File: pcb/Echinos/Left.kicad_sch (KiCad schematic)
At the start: 38 parts, among them J1 USB_C_Receptacle_USB2.0, J2 TagConnect_6pins, J3 Pogo, J4 Conn_01x12_Socket, SW1 SW_Push, SW2 SW_Push, U2 W25Q128JVS, U4 USBLC6-2P6, U5 XC6210B332MR-G

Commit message: ✨ ♻️ 🚧 [PCB] - Continue draft schematic by adding LCSC parts / footprint assignation. Integration of trackball schematic.
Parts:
- added D2: TPD1E10B06-Q1, Diode_SMD:D_SOD-523, symbol Diode:BZT52Bxx
- added U4: ESD7L5.0DT5G-N, Echinos:D_TVS_SOT-723, symbol Power_Protection:TPD2EUSB30
- R1, R10, R11, R13: footprint Resistor_SMD:R_0402_1005Metric_Pad0.72x0.64mm_HandSolder -> Resistor_SMD:R_0805_2012Metric_Pad1.20x1.40mm_HandSolder; LCSC C269746 -> C413739
- SW1: value SW_Push -> Reset
- SW2: value SW_Push -> Bootloader
- renumbered H9 to H6, H6 to H7, H7 to H8, H8 to H9
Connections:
- net Earth is gone; now on an unnamed net: J1.S1 (SHIELD)
- net GND: now also FB1.2, D2.2 (A), U4.3 (GND)
- net USB_D+: now also U4.1 (D+)
- net USB_D-: now also U4.2 (D-)
- net VBUS: now also D2.1 (K)
- net ~{USB_BOOT}: no longer names the net of R5.1, SW2.2
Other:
- added sheet Trackball_Left (Trackball.kicad_sch)
- note added: "1) EMI shield 2) Use a ferrite bead to protect against high frequency 3) Floating to avoid canceling host shield protection Always force a unique path to ground if connected to ground"
- note added: "Bootloader / Reset buttons"
- note added: "ESD protection - VBUS + IO --> ElecSuper USBLC6-2P6-ES (5V, 3 lines, SOT-563) - VBUS --> Texas Instruments TVS0500DRVR (0.39) --> Texas Instruments TPD1E10B06QDPYRQ1 (1.11) - IO --> Born ESD7L5.0DT5G-N (5V, 2 lines, SOT 723) (0.13) --> Texas Instruments TPD2E2U06 (TODO)"
- note added: "Halves communication"
- note added: "I2C Pullers (Optional)"
- note added: "Information"
- note added: "Keyboard matrix"
- note added: "Packaging (metric | imperial) - Resistors - RP2040 --> 1005 | 402 - I2C puller --> 2012 | 805 - Capacitors - RP2040 --> 0402 | 1005 - Diodes - Switches --> SOD-123 - TVS --> SOD-523 - Transistors - ESD --> SOT-723"
- note added: "Trackball (SPI 1)"
- note added: "Trackpad / Trackball (SPI / I2C 0)"
- note removed: "1) Create an all-round contact point between the PCB and the metal housing --> EMI shield 2) Use a ferrite bead to protect against high frequency and force a unique path to ground 3) Avoid any connection (floating) to avoid canceling host shield protection"
- note removed: "??? I2C ???"
- note removed: "Boot / Reset buttons"
- note removed: "Connection between halves"
- note removed: "Matrix"
- note removed: "Trackball / Trackpad (SPI)"
- title: Left Side -> Echinos - Left Side
- moved on the sheet: C14, C18, C19, D1, D2, F1, FB1, H1, H2, H3, H4, H5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

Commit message: ✨ [PCB] - Continue draft schematic by adding per key RGB LED.
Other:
- sheet Matrix_Left ports: added rgb_keys; removed none
- note added: "Keyboard matrix (Keys / LEDs)"
- note added: "Packaging (metric | imperial) - Resistors - RP2040 --> 1005 | 0402 - I2C puller --> 2012 | 0805 - Others --> 1608 | 0603 - Capacitors - RP2040 --> 1005 | 0402 - Others --> 1608 | 0603 - Diodes - Switches --> SOD-123 - TVS --> SOD-523 - Transistors - ESD --> SOT-723"
- note added: "Trackball (SPI 0) --- SPI - motion = Active low interupt line"
- note added: "Trackball sensor directly on the PCB - Minimize the keyboard total height - Enough place for a 34mm ball - Use SPI 1 leaving SPI 0 exposed with the FPC connector"
- note added: "Trackpad (SPI 0 / I2C 0)"
- note added: "Trackpad (SPI 0 / I2C 0) --- SPI - motion = Data Ready (DR) line I2C - Remove R1 on the trackpad PCB"
- note removed: "Keyboard matrix"
- note removed: "Packaging (metric | imperial) - Resistors - RP2040 --> 1005 | 402 - I2C puller --> 2012 | 805 - Capacitors - RP2040 --> 0402 | 1005 - Diodes - Switches --> SOD-123 - TVS --> SOD-523 - Transistors - ESD --> SOT-723"
- note removed: "Trackpad / Trackball (SPI / I2C 0)"
- note removed: "VCC options - 3V and remove R1 to Trackpad PCB - 5V and remove R1/R7/R8 to Trackpad PCB R1 removed --> I2C connection R7/R8 removed --> Support for 5V power"
- note removed: "motion line: - Trackball --> Active low interupt line (motion pin) - Trackpad --> SPI Data ready pin (DR pin)"
- moved on the sheet: D2, H1, H2, H3, H4, H5, H6, H7, H8, H9, J2, J4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

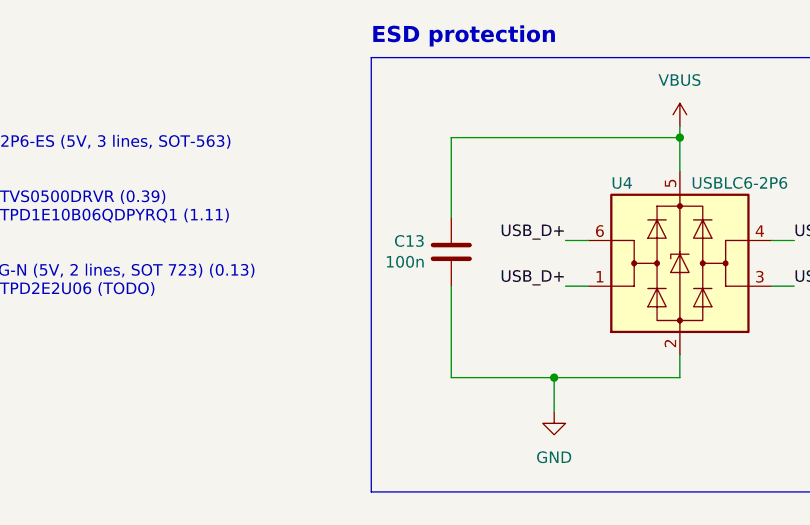
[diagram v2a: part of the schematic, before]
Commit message: ♻️ [PCB] - Remove symbol instances linking to other projets due to copy and paste of component symbol.
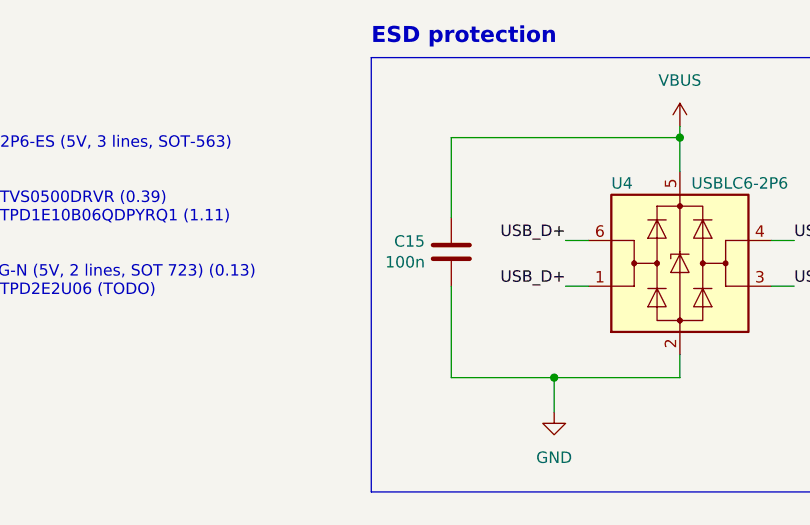
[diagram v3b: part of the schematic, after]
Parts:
- renumbered C13 to C15
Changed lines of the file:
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@@
-        )
-      )
-      (project "ptechinos"
-        (path "/e63e39d7-6ac0-4ffd-8aa3-1841a4541b55"
-          (reference "H1") (unit 1)
         )
       )
@@
   (symbol (lib_id "Device:C") (at -52.07 -48.26 0) (mirror y) (unit 1)
     (in_bom yes) (on_board yes) (dnp no)
-    (property "Reference" "C13" (at -54.991 -49.4284 0)
+    (property "Reference" "C15" (at -54.991 -49.4284 0)
       (effects (font (size 1.27 1.27)) (justify left))
     )
@@
     (pin "2")
     (instances
-      (project "RP2040_minimal"
-        (path "/4f77defa-fbfc-4ef8-94fc-c086dd0772f3"
-          (reference "C13") (unit 1)
-        )
-      )
       (project "Echinos"
         (path "/5bd3006d-ec09-4ffb-bec3-03fa5613b46a"
@@
         )
       )
-      (project "ptechinos"
-        (path "/e63e39d7-6ac0-4ffd-8aa3-1841a4541b55"
-          (reference "H9") (unit 1)
-        )
-      )
     )
   )
@@
         )
       )
-      (project "ptechinos"
-        (path "/e63e39d7-6ac0-4ffd-8aa3-1841a4541b55"
-          (reference "H5") (unit 1)
-        )
-      )
     )
   )
@@
         )
       )
-      (project "ptechinos"
-        (path "/e63e39d7-6ac0-4ffd-8aa3-1841a4541b55"
-          (reference "H2") (unit 1)
-        )
-      )
     )
   )
@@
       (project "Echinos"
         (path "/5bd3006d-ec09-4ffb-bec3-03fa5613b46a/82089e05-aeac-4bc0-b466-29ce28ef1ab1"
-          (reference "H4") (unit 1)
-        )
-      )
-      (project "ptechinos"
-        (path "/e63e39d7-6ac0-4ffd-8aa3-1841a4541b55"
           (reference "H4") (unit 1)
         )
@@
         )
       )
-      (project "ptechinos"
-        (path "/e63e39d7-6ac0-4ffd-8aa3-1841a4541b55"
-          (reference "J7") (unit 1)
-        )
-      )
     )
   )
@@
         )
       )
-      (project "ptechinos"
-        (path "/e63e39d7-6ac0-4ffd-8aa3-1841a4541b55"
-          (reference "H3") (unit 1)
-        )
-      )
     )
   )
@@
         )
       )
-      (project "ptechinos"
-        (path "/e63e39d7-6ac0-4ffd-8aa3-1841a4541b55"
-          (reference "H7") (unit 1)
-        )
-      )
     )
   )
@@
       (project "Echinos"
         (path "/5bd3006d-ec09-4ffb-bec3-03fa5613b46a/82089e05-aeac-4bc0-b466-29ce28ef1ab1"
-          (reference "H8") (unit 1)
-        )
-      )
-      (project "ptechinos"
-        (path "/e63e39d7-6ac0-4ffd-8aa3-1841a4541b55"
           (reference "H8") (unit 1)
         )
@@
           (reference "H6") (unit 1)
         )
-      )
-      (project "ptechinos"
-        (path "/e63e39d7-6ac0-4ffd-8aa3-1841a4541b55"
-          (reference "H6") (unit 1)
-        )

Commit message: ♻️ [PCB] - Add ferrite bead between shield and ground. Assign hand solder footprints whenever possible. Complete footprint assignation.
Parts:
- C14, C18, C19: footprint Capacitor_SMD:C_0603_1608Metric -> Capacitor_SMD:C_0603_1608Metric_Pad1.08x0.95mm_HandSolder
- C15: footprint Capacitor_SMD:C_0402_1005Metric -> Capacitor_SMD:C_0402_1005Metric_Pad0.74x0.62mm_HandSolder
- D1: footprint (none) -> Diode_SMD:D_SOD-323_HandSoldering
- D2: footprint Diode_SMD:D_SOD-323 -> Diode_SMD:D_SOD-323_HandSoldering
- F1: footprint Fuse:Fuse_0603_1608Metric -> Fuse:Fuse_0603_1608Metric_Pad1.05x0.95mm_HandSolder
- FB1: value FerriteBead_Small -> 80@100Mhz; footprint (none) -> Inductor_SMD:L_0805_2012Metric_Pad1.15x1.40mm_HandSolder; LCSC C98288 -> C12389
- J1: footprint (none) -> Connector_USB:USB_C_Receptacle_HRO_TYPE-C-31-M-12; LCSC (none) -> C165948
- JP1, JP2: footprint (none) -> Echinos:SolderJumper_Open_0.8x1.2mm
- R2, R3, R4, R5, R9: footprint Resistor_SMD:R_0402_1005Metric -> Resistor_SMD:R_0402_1005Metric_Pad0.72x0.64mm_HandSolder
- U5: footprint Package_TO_SOT_SMD:SOT-23-5 -> Package_TO_SOT_SMD:SOT-23-5_HandSoldering
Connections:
- net +5V: now also D2.1 (K)
- net GND: now also FB1.1; no longer FB1.2
- net VBUS: no longer D2.1 (K), F1.1, J1.A4 (VBUS), J1.A9 (VBUS), J1.B4 (VBUS), J1.B9 (VBUS)
- net Earth: now reaches J1.S1 (SHIELD)
- net Earth: now also FB1.2; no longer FB1.1
- new net: F1.1, J1.A4 (VBUS), J1.A9 (VBUS), J1.B4 (VBUS), J1.B9 (VBUS)
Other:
- note added: "Design rules ---------"
- note added: "Filter ESD (100-500Mhz) Filter high frequency noise Impedance should be in 50-100Ω range at 100Mhz Impedance drop quickly when moving toward ferrite current rating --> I_Circuit ~= 0.2 x I_CR Continue USB Shield using metalic case / plate to create a 360° protection Connect Shield and Ground in only one location (keep out one under USB)"
- note added: "Packaging (metric | imperial) - Resistors - RP2040 --> 1005 | 0402 - USB data --> 1005 | 0402 - I2C puller --> 2012 | 0805 - Others --> 1608 | 0603 - Capacitors - RP2040 --> 1005 | 0402 - Others --> 1608 | 0603 - Diodes - Switches --> SOD-123 - TVS --> SOD-523 - Transistors - ESD --> SOT-723"
- note added: "Tells host that we need 500mA"
- note removed: "1) EMI shield 2) Use a ferrite bead to protect against high frequency 3) Floating to avoid canceling host shield protection Always force a unique path to ground if connected to ground"
- note removed: "Packaging (metric | imperial) - Resistors - RP2040 --> 1005 | 0402 - I2C puller --> 2012 | 0805 - Others --> 1608 | 0603 - Capacitors - RP2040 --> 1005 | 0402 - Others --> 1608 | 0603 - Diodes - Switches --> SOD-123 - TVS --> SOD-523 - Transistors - ESD --> SOT-723"
- moved on the sheet: D2, F1, J1, R2, R3

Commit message: ✨ 🐛 ✅ [PCB] - Pass ERC test (exception to unconnected GPIO pins). Fix power symbol assignation to please Kicad. Fix duplicated line name (encoder / joystick) to please Kicad. Add trackball sensor connection documentation. Assign newly created footprints (encoder, joystick, switch).
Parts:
- removed C15: 100n, Capacitor_SMD:C_0402_1005Metric_Pad0.74x0.62mm_HandSolder, symbol Device:C
- removed U4: USBLC6-2P6, Package_TO_SOT_SMD:SOT-666, symbol Power_Protection:USBLC6-2P6
- H6: symbol ptechinos:Mount_Tenting -> Echinos:Mount_Tenting; now in the parts list
- J3: footprint Echinos:Pogo_1x04_P2.5mm -> Echinos:Pogo_RightAngle_1x04_P2.5mm
- SW1: value Reset -> SW_Push
- SW2: value Bootloader -> SW_Push
- renumbered U4 to U3
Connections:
- net +3V3 is gone; now on net +3.3V: C19.1, J3.1 (Pin_1), J4.12 (Pin_12), JP1.1 (A), JP2.1 (A), R12.2, R9.1, U5.5 (VOUT)

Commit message: ✨ [PCB] - Complete schema and PCB for left halve. All connections are made. Optional encoder on the top outer key Optional joystick on either outer thumb or above middle thumb. Optional power LED (jumpers) SATA to connect both sides VIK compatible (except for 5.0V track) with enough space on the inner side to clip a VIK module Remaining MCU pins exposed with a 2.54mm spaced header All VIK modules are not yet placed / routed.
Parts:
- removed H6: Mount_Tenting, Echinos:Tenting_Puck, symbol Echinos:Mount_Tenting
- removed J3: Pogo, Echinos:Pogo_RightAngle_1x04_P2.5mm, symbol Connector_Generic:Conn_01x04
- added FB1: 80@100Mhz, Inductor_SMD:L_0805_2012Metric_Pad1.15x1.40mm_HandSolder, symbol Device:FerriteBead_Small
- added J205: ~, symbol Vik:vik-module-connector
- added J206: Conn_01x06_Pin, Connector_PinHeader_2.54mm:PinHeader_1x06_P2.54mm_Vertical, symbol Connector:Conn_01x06_Pin
- added J301: SATA-7p, Echinos:SATA_1x07_P1.27mm_SMD, symbol Echinos:SATA-7p
- added JP2: 3x3_LED_jumper, Echinos:SolderJumper_Open_0.8x1.2mm, symbol Jumper:SolderJumper_2_Open
- added U7: D3V3F4U6S-7, Echinos:D_TVS_SOT-363, symbol Echinos:D3V3F4U6S-7
- H1, H2, H3, H4, H5: footprint MountingHole:MountingHole_3.2mm_M3_Pad_Via -> Echinos:MountingHole_3mm_Pad_Via; symbol Mechanical:MountingHole -> Mechanical:MountingHole_Pad
- J4: value Conn_01x12_Socket -> FPC_VIK
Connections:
- net +3.3V: now also J4.1 (Pin_1), J205.12 (3V3), J206.2 (Pin_2), J301.2 (S2), J301.3 (S3), JP2.1 (A), U7.2 (VN); no longer J4.12 (Pin_12), R12.2
- net GND: now also H1.1, H2.1, H3.1, H4.1, H5.1, J4.2 (Pin_2), SW1.2, FB1.2, J205.11 (GND), J206.1 (Pin_1), J301.1 (S1), J301.4 (S4), J301.7 (S7), U7.5 (VP); no longer J4.11 (Pin_11), SW1.1
- net USB_D+: now also U3.2 (D+); no longer U3.1 (D+)
- net USB_D-: now also U3.1 (D-); no longer U3.2 (D-)
- net adc_2: now also J4.9 (Pin_9), J205.4 (GPIO_AD2)
- net adc_3: now also J4.7 (Pin_7), J205.6 (GPIO_AD1)
- net csn0: now also J206.6 (Pin_6); no longer J4.3 (Pin_3)
- net csn1: now also J4.10 (Pin_10), J205.3 (SPI_CS)
- net miso0: now also J206.5 (Pin_5); no longer J4.2 (Pin_2)
- net miso1: now also J4.11 (Pin_11), J205.2 (MISO)
- net mosi0: now also J206.4 (Pin_4); no longer J4.5 (Pin_5)
- net mosi1: now also J4.8 (Pin_8), J205.5 (MOSI)
- net motion: no longer J4.4 (Pin_4)
- net sck0: now also J206.3 (Pin_3); no longer J4.1 (Pin_1)
- net sck1: now also J4.12 (Pin_12), J205.1 (SCLK)
- net scl0: no longer J4.9 (Pin_9)
- net scl1: now also J4.4 (Pin_4), J205.9 (SCL)
- net sda0: no longer J4.10 (Pin_10)
- net sda1: now also J4.3 (Pin_3), J205.10 (SDA)
- net ~{RST}: now also SW1.1; no longer SW1.2
- net VBUS: now reaches F1.1, J1.A4 (VBUS), J1.A9 (VBUS), J1.B4 (VBUS), J1.B9 (VBUS)
- new net: JP2.2 (B), R12.2
- new net: FB1.1, J301.SH1 (SHIELD), J301.SH2 (SHIELD)
- new net RX: J301.5 (S5), U7.1 (CH1), U7.3 (CH2)
- new net TX: J301.6 (S6), U7.4 (CH3), U7.6 (CH4)
- new net rgb: J205.8 (RGB_LED_IN), J4.5 (Pin_5)
- no-connect marks 7 -> 5
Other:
- sheet Matrix_Left ports: added backlights; removed rgb_keys
- sheet RP2040_Left ports: added GPIO4, VBUS_DET; removed GPI04, GPIO7
- note added: "EMI Shield / Case mounting holes"
- note added: "ESD protection (USB + SATA)"
- note added: "I2C --> Remove R1 on the trackpad PCB"
- note added: "Resistor must be close to the flash chip Switch pushed (low) --> Bootloader Switch released (pulled high) --> Firmware"
- note added: "SATA (3.3V, USART)"
- note added: "Trackpad (SPI 1 or I2C 1)"
- note added: "USART full duplex RX_left <-- TX_right TX_left --> RX_right"
- note added: "USB (5.5V, Data)"
- note added: "Unused MCU pins"
- note added: "VIK compatible - Cirque compatible with FPC Type A cable (reverse pins) ?? 5V is a waste pin that could be used to expose another IO ?? ?? - Could be useful with a joystick ??"
- note added: "VIK connector (SPI 1 / I2C 1)"
- note added: "VIK modules"
- note removed: "??? EMI Shield / Case mounting holes ???"
- note removed: "??? OLED / LCD ???"
- note removed: "??? TRRS ???"
- note removed: "ESD protection"
- note removed: "Resistor must be close to the flash chip Switch pushed (low) --> USB Bootloader Switch released (pulled high) --> Firmware"
- note removed: "Trackball sensor directly on the PCB - Minimize the keyboard total height - Enough place for a 34mm ball - Use SPI 1 leaving SPI 0 exposed with the FPC connector"
- note removed: "Trackpad (SPI 0 / I2C 0)"
- moved on the sheet: D1, D2, H7, H8, H9, J4, JP1, JP2, R1, R10, R11, R12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

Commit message: 🚧 [PCB] - Backup of a specific layout around MCU. Modules moved to a specific schematic page.
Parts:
- removed H7, H8, H9: GuardHole, MountingHole:MountingHole_2.2mm_M2_Pad_Via, symbol Mechanical:MountingHole
- removed J205: ~, symbol Vik:vik-module-connector
- added J208: FPC (PCB), Connector_FFC-FPC:Hirose_FH12-12S-0.5SH_1x12-1MP_P0.50mm_Horizontal, symbol Connector:Conn_01x12_Socket
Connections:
- net +3.3V: now also J208.11 (Pin_11)
- net GND: now also J208.12 (Pin_12)
- net adc_0: now also J208.9 (Pin_9)
- net adc_1: now also J208.7 (Pin_7)
- net col1: now also J208.1 (Pin_1)
- net col2: now also J208.2 (Pin_2)
- net col3: now also J208.3 (Pin_3)
- net col4: now also J208.4 (Pin_4)
- net col5: now also J208.6 (Pin_6)
- net rgb: now also J208.8 (Pin_8)
- new net row5: J208.5 (Pin_5)
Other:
- removed sheet Trackball_Left
- note added: "EMI Shield Case mounting holes"
- note added: "Expansion connector (Matrix / ADC)"
- note added: "Matrix diodes must be added on the module side."
- note added: "Matrix expansion - Add 5 way joystick - Add mouse buttons - ..."
- note added: "Unused MCU pins (Optional)"
- note removed: "??? Design / Artist ???"
- note removed: "EMI Shield / Case mounting holes"
- note removed: "I2C --> Remove R1 on the trackpad PCB"
- note removed: "Trackball (SPI 0) --- SPI - motion = Active low interupt line"
- note removed: "Trackball (SPI 1)"
- note removed: "Trackpad (SPI 0 / I2C 0) --- SPI - motion = Data Ready (DR) line I2C - Remove R1 on the trackpad PCB"
- note removed: "Trackpad (SPI 1 or I2C 1)"
- note removed: "Unused MCU pins"
- note removed: "VIK modules"
- moved on the sheet: H1, H2, H3, H4, H5, J2, J206, J4, JP1, JP2, R1, R10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
